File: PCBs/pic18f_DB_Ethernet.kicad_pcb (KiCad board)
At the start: 2 copper layers, 29 parts, among them J1 OC1, J2 PicKIT 3, J3 IC1, J4 FC1, J5 MC1, J6 DB9_Female, J7 DB9_Male, J8 RJ45, U1 pic18f45k20

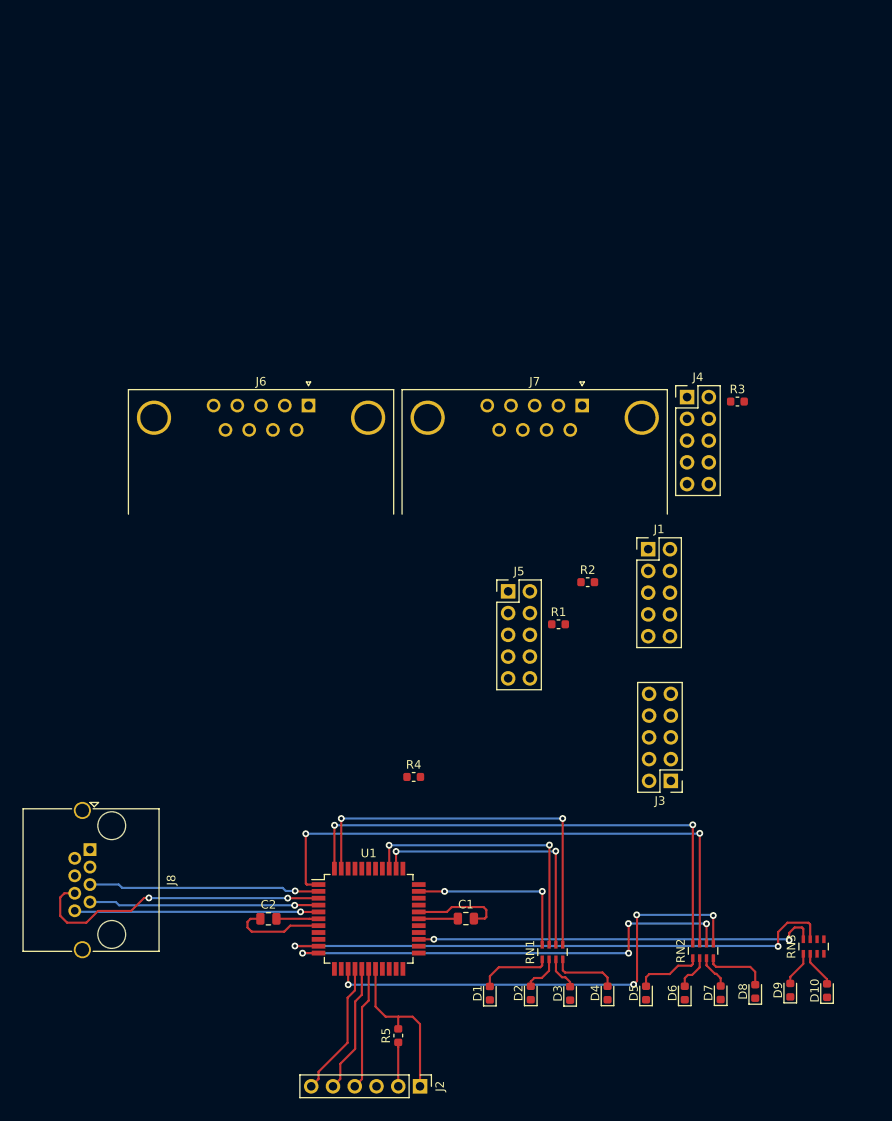
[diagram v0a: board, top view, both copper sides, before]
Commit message: Basic routing of known components complete. TODO: Outline, mouse bites, missing parts
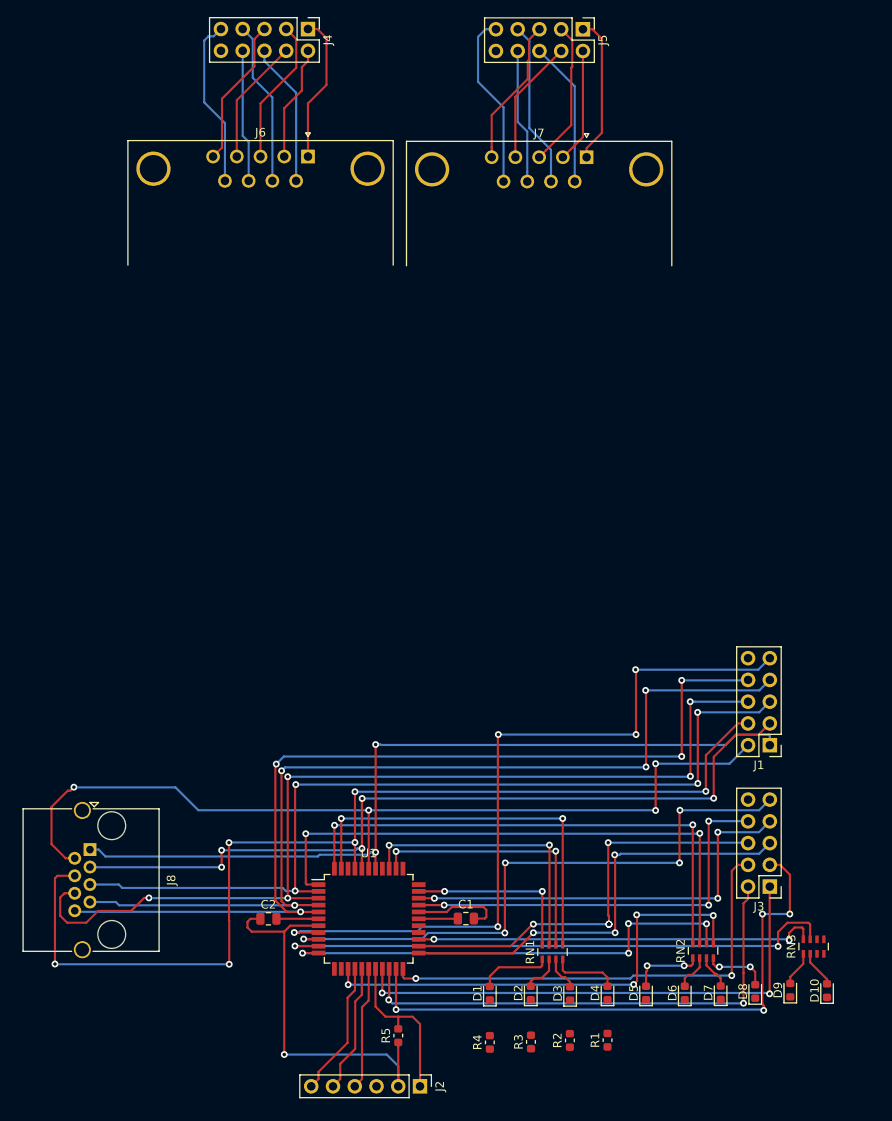
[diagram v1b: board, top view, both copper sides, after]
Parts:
- moved R3 78.6 mm to (159.9, 140.2), turned to 90 degrees
- moved J5 66.2 mm to (166.0, 21.9), turned to 270 degrees
- moved J4 61.7 mm to (133.9, 21.9), turned to 270 degrees
- moved R2 53.5 mm to (164.5, 140.0), turned to 90 degrees
- moved R1 48.9 mm to (168.9, 140.0), turned to 90 degrees
- moved R4 32.2 mm to (155.1, 140.2), turned to 90 degrees
- moved J6 29.1 mm to (133.9, 36.8)
- moved J7 29.0 mm to (166.4, 36.9)
- moved J1 26.9 mm to (187.8, 105.5), turned to 180 degrees
- moved J3 16.9 mm to (187.8, 122.0)
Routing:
- net In4: track 0.00 -> 122.4 mm, vias 0 -> 6
- net In2: track 0.00 -> 104.3 mm, vias 0 -> 4
- net In3: track 0.00 -> 96.1 mm, vias 0 -> 5
- net In1: track 0.00 -> 96.1 mm, vias 0 -> 2
- net In9: track 0.00 -> 89.2 mm, vias 0 -> 5
- net In8: track 28.5 -> 112.3 mm, vias 1 -> 4
- net In7: track 26.9 -> 110.5 mm, vias 1 -> 4
- net In5: track 27.0 -> 103.7 mm, vias 1 -> 4
- net In6: track 35.8 -> 112.4 mm, vias 2 -> 5
- net Out9: track 0.00 -> 71.3 mm, vias 0 -> 5
- net Out3: track 0.00 -> 69.6 mm, vias 0 -> 4
- net Out1: track 0.00 -> 60.6 mm, vias 0 -> 2
- net Out2: track 0.00 -> 59.1 mm, vias 0 -> 2
- net Out4: track 0.00 -> 54.0 mm, vias 0 -> 2
- net Out5: track 0.00 -> 51.7 mm, vias 0 -> 3
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
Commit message: Added dpdt switch from stock. added battery clip. Reconsidering mouser bites. TODO: Orthagonal repo of parts rendered in KiCAD.
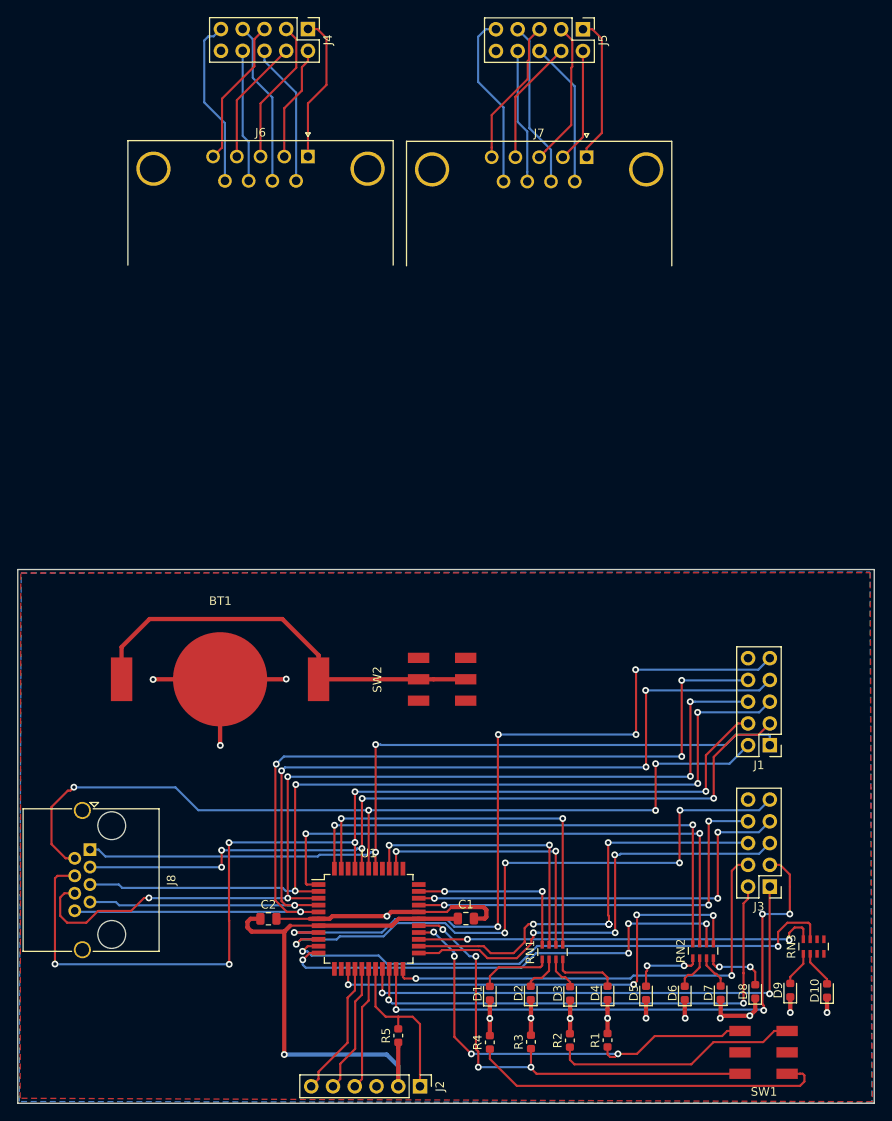
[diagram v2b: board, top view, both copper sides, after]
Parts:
- added BT1: CR2032, BAT-HLD-001:BAT-HLD-001, F.Cu at (123.6, 97.8)
- added SW1: SW_DPDT_x2, JS202011SCQN:JS202011SCQN, F.Cu at (187.1, 141.4)
- added SW2: PWR_SW, JS202011SCQN:JS202011SCQN, F.Cu at (149.5, 97.8)
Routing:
- net GND: track 15.5 -> 83.1 mm, vias 0 -> 14
- net SW0: track 0.00 -> 54.3 mm, vias 0 -> 4
- net SW1: track 0.00 -> 52.6 mm, vias 0 -> 4
- net Net-(BT1-Pad1): track 0.00 -> 49.9 mm
- net Net-(R4-Pad1): track 0.00 -> 42.2 mm
- net Net-(R2-Pad1): track 0.00 -> 28.7 mm
- net 3v3: track 51.4 -> 63.4 mm
- net Out9: track 71.3 -> 74.4 mm
- net Led7: track 54.9 -> 56.5 mm
- net Out6: track 49.2 -> 50.8 mm
- net Out5: track 51.7 -> 53.1 mm
- net In9: track 89.2 -> 90.0 mm
- added copper zone on F.Cu, net 3v3
- added copper zone on B.Cu, net GND
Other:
- board outline added: 100 x 62.3 mm
- net class PWR added: clearance 0.2, trace_width 0.5, via_dia 0.8, via_drill 0.4

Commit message: Finished Rev A layout. Some research revealed that JLCPCB does not support what I want. I might just send the break out into a different pcb.
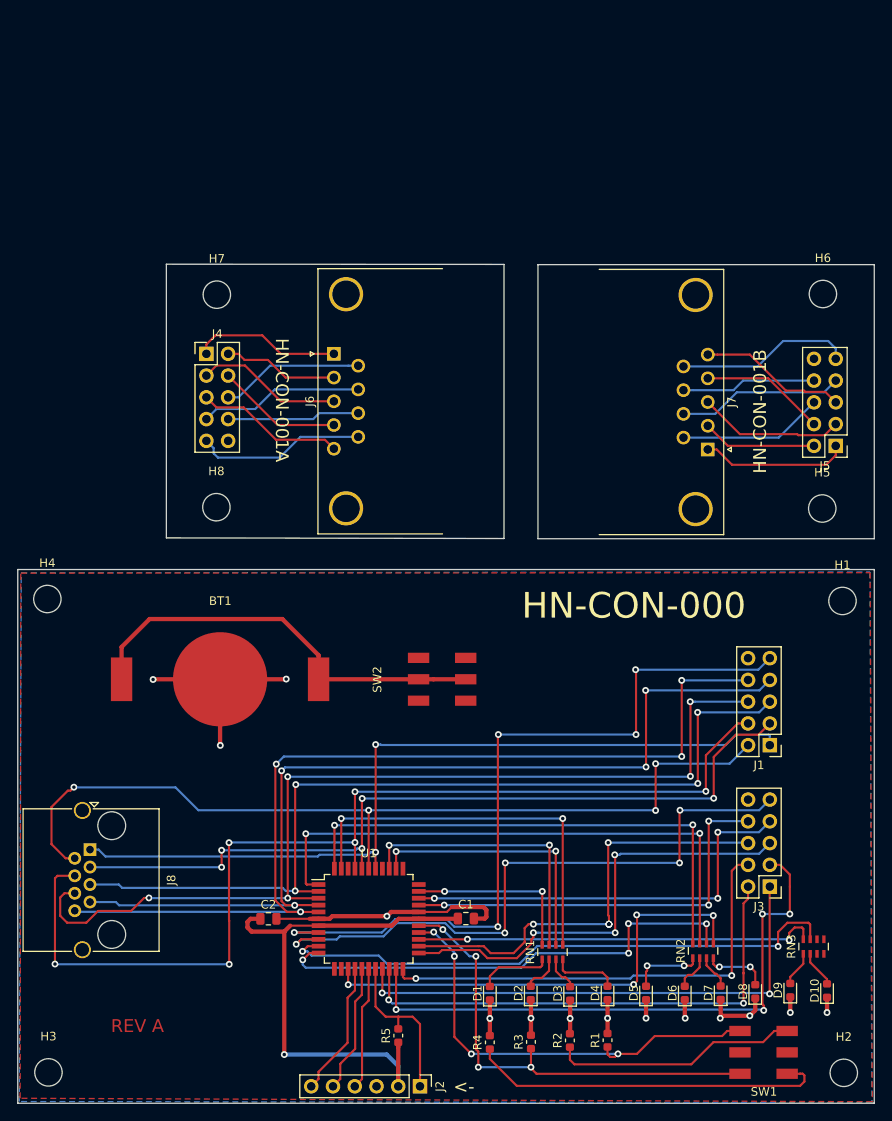
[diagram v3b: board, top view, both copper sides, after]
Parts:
- added H1: MountingHole, MountingHole:MountingHole_3.2mm_M3, F.Cu at (196.3, 88.7)
- added H2: MountingHole, MountingHole:MountingHole_3.2mm_M3, F.Cu at (196.4, 143.8)
- added H3: MountingHole, MountingHole:MountingHole_3.2mm_M3, F.Cu at (103.6, 143.7)
- added H4: MountingHole, MountingHole:MountingHole_3.2mm_M3, F.Cu at (103.5, 88.4)
- added H5: MountingHole, MountingHole:MountingHole_3.2mm_M3, F.Cu at (193.9, 77.9)
- added H6: MountingHole, MountingHole:MountingHole_3.2mm_M3, F.Cu at (194.0, 52.8)
- added H7: MountingHole, MountingHole:MountingHole_3.2mm_M3, F.Cu at (123.2, 52.9)
- added H8: MountingHole, MountingHole:MountingHole_3.2mm_M3, F.Cu at (123.2, 77.7)
- moved J5 56.9 mm to (195.5, 70.6), turned to 180 degrees
- moved J4 39.7 mm to (122.0, 59.8), turned to 0 degrees
- moved J7 36.9 mm to (180.6, 71.0), turned to 270 degrees
- moved J6 23.2 mm to (136.9, 59.8), turned to 90 degrees
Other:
- board size 100 x 62.3 mm -> 100 x 98 mm
- board text added: "<-"
- board text added: "HN-CON-000"
- board text added: "HN-CON-001A"
- board text added: "HN-CON-001B"
- board text added: "REV A"

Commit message: Restructed project
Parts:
- removed H5, H6, H7, H8: MountingHole, MountingHole:MountingHole_3.2mm_M3
- removed J4: FC1, Connector_PinHeader_2.54mm:PinHeader_2x05_P2.54mm_Vertical
- removed J5: MC1, Connector_PinHeader_2.54mm:PinHeader_2x05_P2.54mm_Vertical
- removed J6: DB9_Female, Connector_Dsub:DSUB-9_Female_Horizontal_P2.77x2.84mm_EdgePinOffset9.90mm_Housed_MountingHolesOffset11.32mm
- removed J7: DB9_Male, Connector_Dsub:DSUB-9_Female_Horizontal_P2.77x2.84mm_EdgePinOffset9.90mm_Housed_MountingHolesOffset11.32mm
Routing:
- net M9: track 20.6 -> 0.00 mm
- net F9: track 19.9 -> 0.00 mm
- net M7: track 19.4 -> 0.00 mm
- net F7: track 19.2 -> 0.00 mm
- net F5: track 17.4 -> 0.00 mm
- net F1: track 17.3 -> 0.00 mm
- net M5: track 17.2 -> 0.00 mm
- net M1: track 17.2 -> 0.00 mm
- net F3: track 17.1 -> 0.00 mm
- net M3: track 17.1 -> 0.00 mm
- net M6: track 16.9 -> 0.00 mm
- net F6: track 16.7 -> 0.00 mm
- net M8: track 15.7 -> 0.00 mm
- net F8: track 15.5 -> 0.00 mm
- net F4: track 14.7 -> 0.00 mm
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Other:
- board size 100 x 98 mm -> 100 x 62.3 mm
- board text removed: "HN-CON-001A"
- board text removed: "HN-CON-001B"

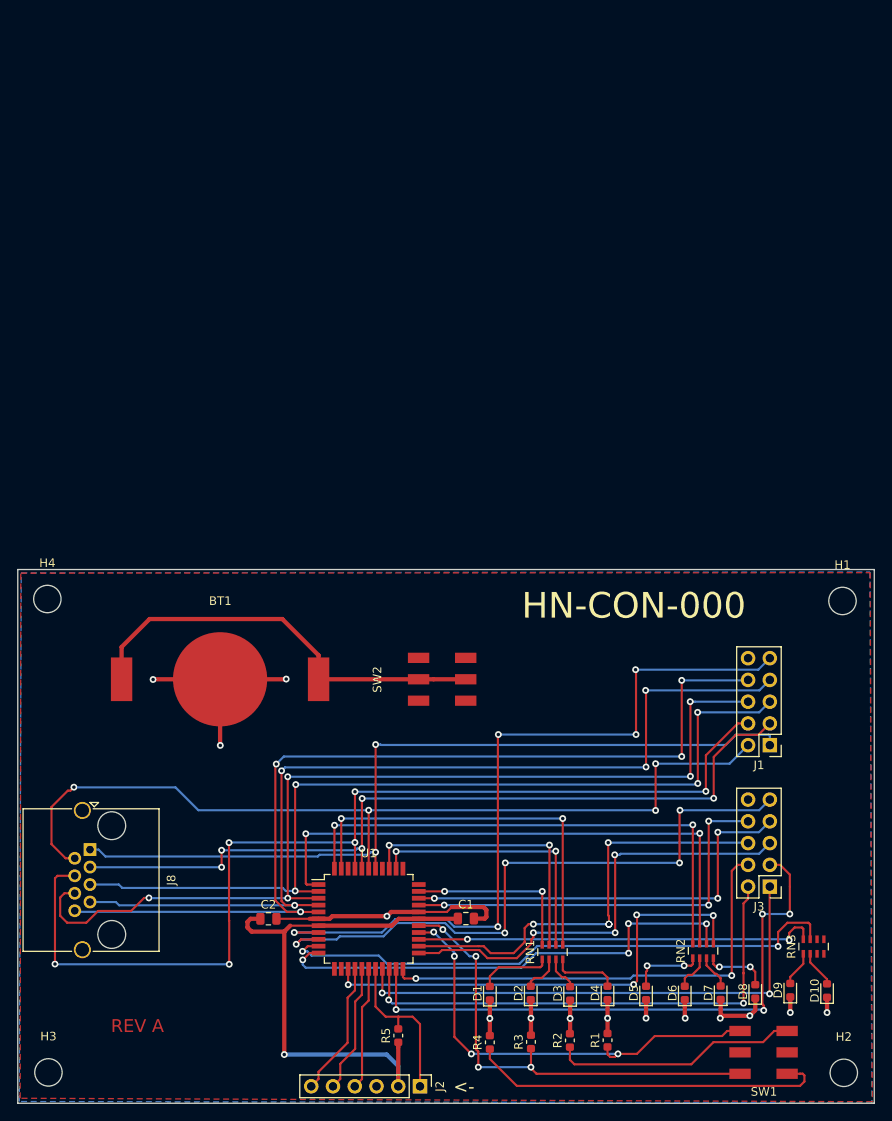
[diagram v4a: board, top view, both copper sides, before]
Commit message: Minor rerouting to address power trace width. Added OSHW logo. Updated todo list
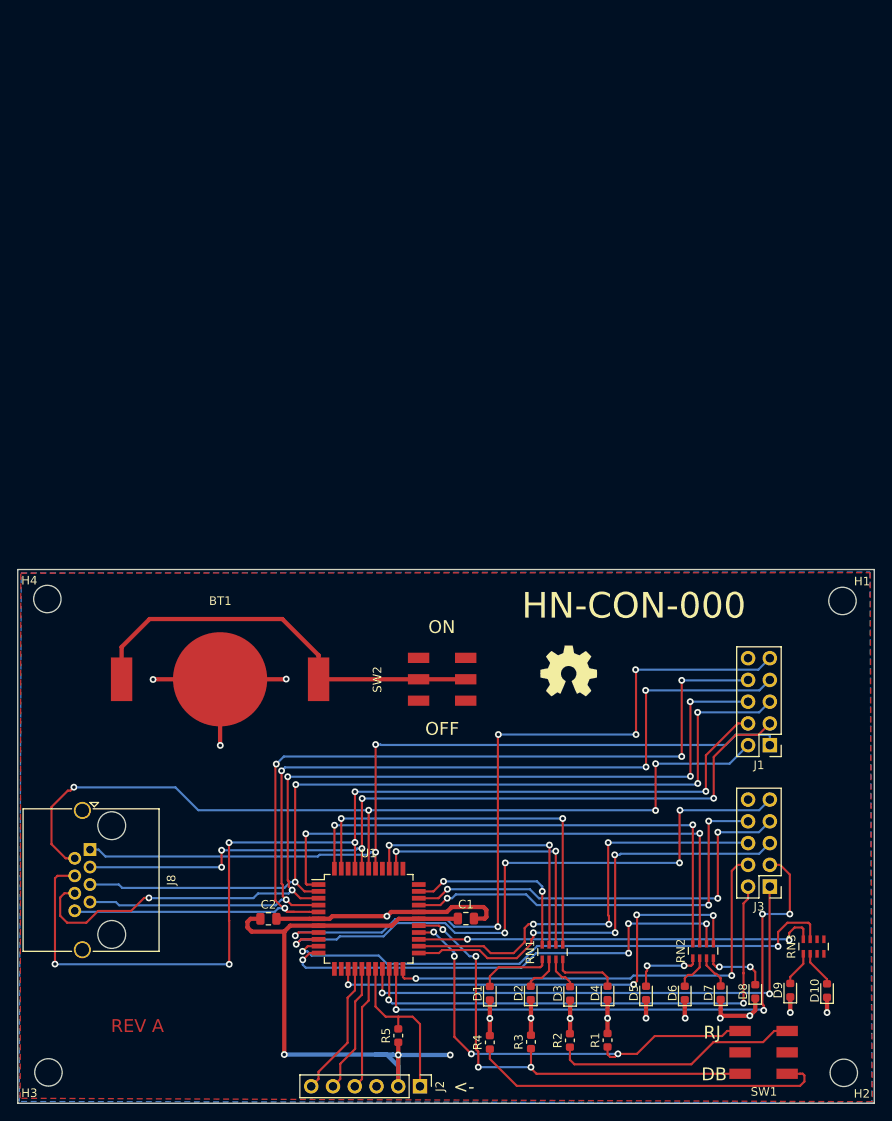
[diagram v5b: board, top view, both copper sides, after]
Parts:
- added REF**: OSHW-Symbol_6.7x6mm_SilkScreen, Symbol:OSHW-Symbol_6.7x6mm_SilkScreen, F.Cu at (164.3, 96.9)
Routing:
- net 3v3: track 63.4 -> 75.8 mm, vias 1 -> 3
- net Led1: track 20.7 -> 22.0 mm
- net In7: track 110.5 -> 109.4 mm
- net Out8: track 48.3 -> 49.3 mm
- net Out7: track 49.2 -> 50.1 mm
- net Out6: vias 5 -> 3
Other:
- board text added: "DB"
- board text added: "OFF"
- board text added: "ON"
- board text added: "RJ"

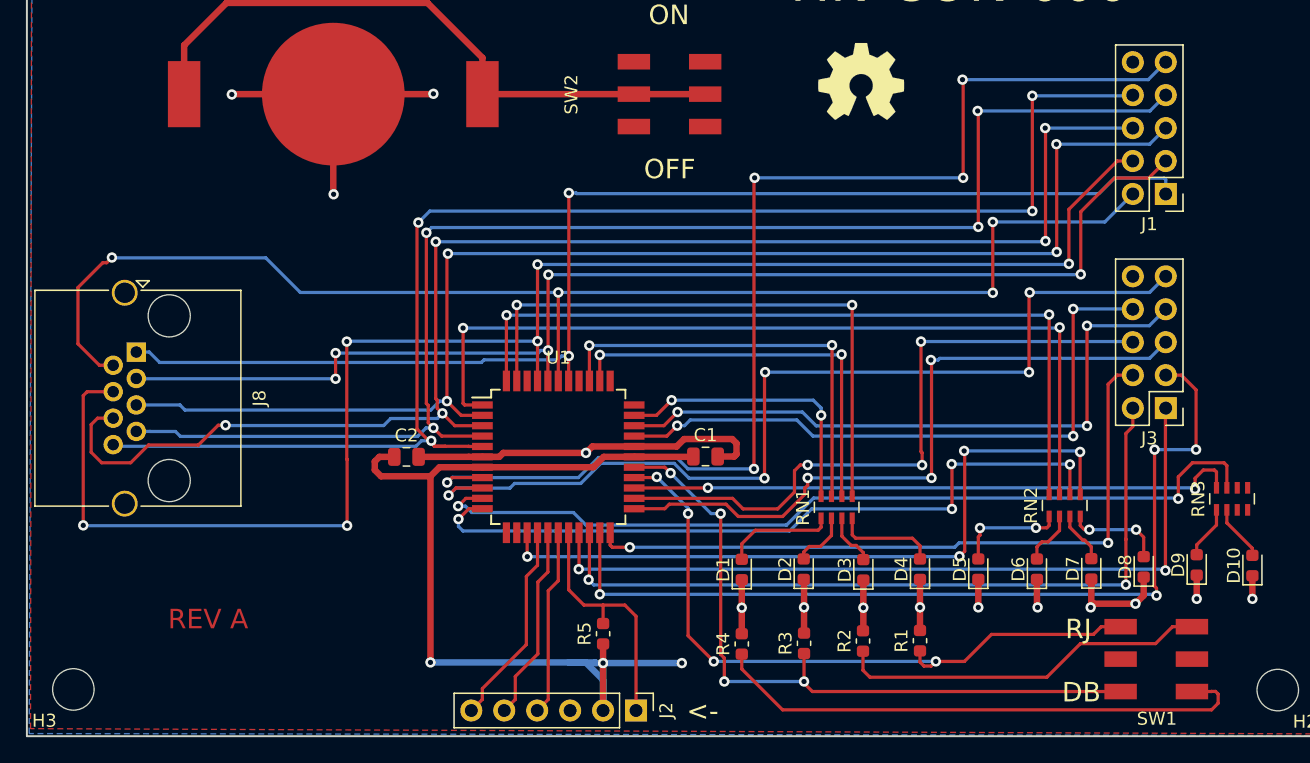
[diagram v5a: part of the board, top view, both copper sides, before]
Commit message: changed RJ45 jack to unsheilded. Printed main board gerbers and gerber pdfs
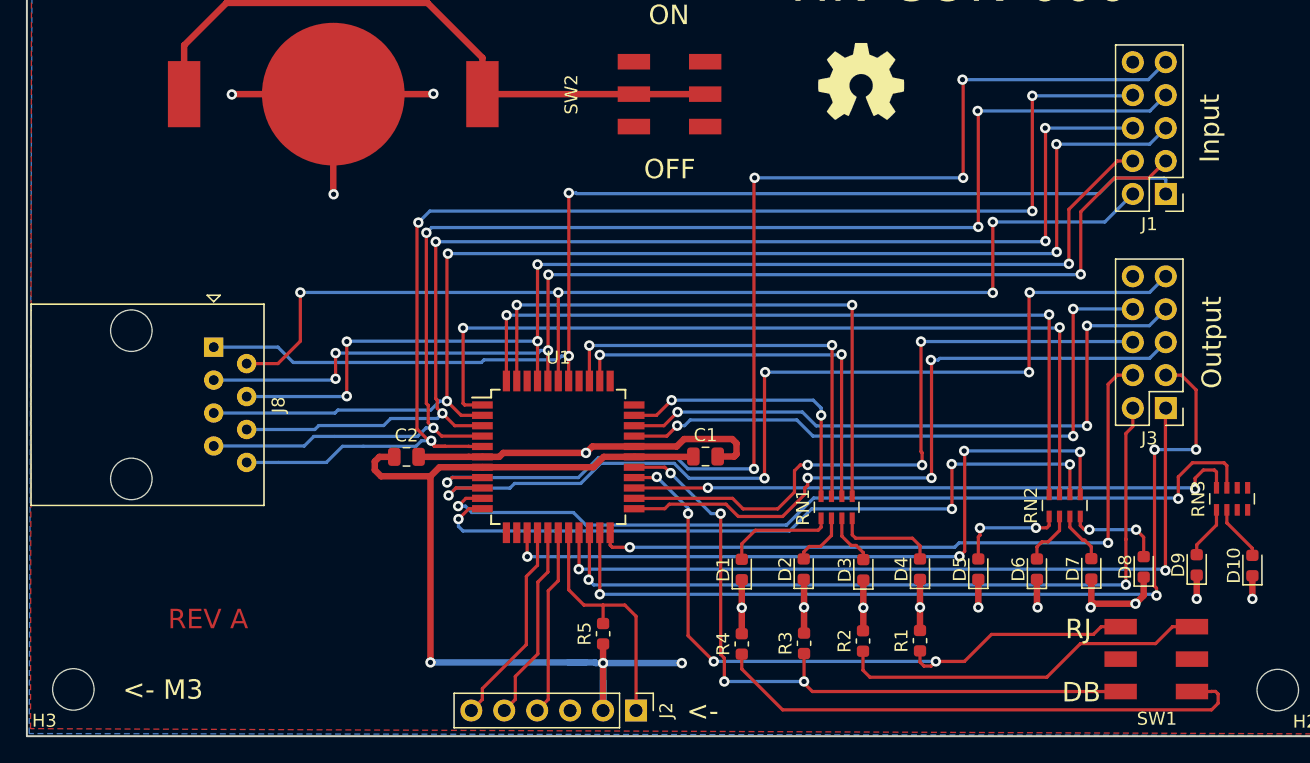
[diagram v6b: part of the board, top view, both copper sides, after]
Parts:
- J8: footprint Connector_RJ:RJ45_Amphenol_RJHSE5380 -> Connector_RJ:RJ45_Amphenol_54602-x08_Horizontal
- moved J8 5.98 mm to (114.4, 117.3)
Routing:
- net In4: track 122.4 -> 87.3 mm, vias 6 -> 5
- net In2: track 104.3 -> 86.0 mm
- net In6: track 112.5 -> 95.1 mm, vias 5 -> 4
- net In8: track 111.9 -> 102.0 mm
- net In5: track 103.3 -> 97.2 mm
- net In3: track 96.1 -> 90.2 mm
- net In7: track 109.4 -> 103.5 mm
- net In1: track 96.1 -> 90.3 mm
- net 3v3: track 75.8 -> 73.9 mm
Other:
- board text added: "<- M3"
- board text added: "Input"
- board text added: "Output"
